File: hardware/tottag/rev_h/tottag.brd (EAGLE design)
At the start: 68.1 x 39.6 mm, 203 parts, among them J1 USB4110-GF-A, J2 DM3AT-SF-PEJM5, J3 TC2030-JLINK-NL-2SIDE, J4 TC2030-JLINK-NL-2SIDE, J5 MOLEX-PICO-SPOX-3SIDE, Q1 CSD75207W15, Q2 CSD75207W15, T1 HHM1595A1, U1 DW1000, U10 STM32F091CC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

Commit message: rev_h: split SPI buses; replace coil
Pin updates from SPI reconfiguration:

    SPI0 (Accelerometer)
        SCLK: P0.17
        MISO: P0.15
        MOSI: P0.13
        (INT, CS pins unchanged)
    SPI2 (RTC, SD Card)
        SCLK: P0.06
        MOSI: P0.07
        MISO: P0.05
        (CS, detect, etc pins unchanged)
    BATIN moved to P0.04 (to simplify routing)

---

Coil replaced with new part; slightly wider holes, adjusted fill to fit

(was meant to be its own commit; oh well)
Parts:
- L4: value WR222230-26M8-G -> WURTH_COIL_760308103204; device ac:WR222230-26M8-G -> ac:WURTH_COIL_760308103204
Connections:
- removed net NRF_MISO: J2.7, R32.1, U11.6, U3.3, U7.AD10
- removed net NRF_MOSI: J2.3, R30.1, U11.9, U3.4, U7.AD8
- removed net NRF_SCK: J2.5, U11.7, U3.1, U7.AD12
- new net NRF_SPI0_MISO: U3.3, U7.AD10
- new net NRF_SPI0_MOSI: U3.4, U7.AD8
- new net NRF_SPI0_SCLK: U3.1, U7.AD12
- new net NRF_SPI2_MISO: J2.7, R32.1, U11.6, U7.K2
- new net NRF_SPI2_MOSI: J2.3, R30.1, U11.9, U7.M2
- new net NRF_SPI2_SCLK: J2.5, U11.7, U7.L1
- net BATIN: now also U7.J1; no longer U7.B9
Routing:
- net NRF_MOSI: track 67.9 -> 0.00 mm, vias 11 -> 0
- net NRF_MISO: track 67.8 -> 0.00 mm, vias 5 -> 0
- net NRF_SCK: track 62.0 -> 0.00 mm, vias 8 -> 0
- net NRF_SPI2_MOSI: track 0.00 -> 56.0 mm, vias 0 -> 9
- net NRF_SPI2_MISO: track 0.00 -> 49.1 mm, vias 0 -> 4
- net NRF_SPI2_SCLK: track 0.00 -> 46.4 mm, vias 0 -> 6
- net NRF_SPI0_MOSI: track 0.00 -> 10.7 mm, vias 0 -> 2
- net NRF_SPI0_SCLK: track 0.00 -> 10.3 mm, vias 0 -> 2
- net NRF_SPI0_MISO: track 0.00 -> 10.2 mm, vias 0 -> 2
- net !NRF_CS_IMU: track 11.7 -> 7.53 mm, vias 4 -> 2
- net BATIN: track 30.3 -> 26.9 mm
- net !NRF_RST: track 30.4 -> 28.9 mm
- net STM_INTERRUPT: track 11.5 -> 12.1 mm

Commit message: rev_h: separate debugging headers; also LEDs
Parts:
- moved J4 8.67 mm to (29.1, -2.69), turned to 0 degrees
- moved D2 8.41 mm to (28.4, 7.21), turned to 270 degrees
- moved D3 1.63 mm to (28.4, 0.25)
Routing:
- net N$60: track 35.6 -> 23.2 mm, vias 3 -> 2
- net N$61: track 34.2 -> 22.4 mm
- net N$59: track 35.5 -> 25.3 mm, vias 4 -> 3
- net !STM_RST: track 33.4 -> 42.8 mm, vias 2 -> 3
- net STM_SWDCLK: track 23.3 -> 30.0 mm
- net N$24: track 32.1 -> 25.4 mm
- net STM_SWDIO: track 29.3 -> 35.5 mm
- net N$23: track 29.0 -> 22.9 mm
- net GND: track 185.9 -> 191.3 mm, vias 553 -> 551
- net N$25: track 29.2 -> 24.7 mm
- net !NRF_RST: track 28.9 -> 31.7 mm, vias 4 -> 3
- net NRF_SWDIO: track 32.5 -> 29.7 mm, vias 2 -> 1
- net +3V3: track 145.3 -> 147.9 mm, vias 42 -> 46
- net NRF_SWDCLK: track 26.4 -> 28.7 mm, vias 2 -> 1
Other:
- outline, holes or cut-outs redrawn

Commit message: rev_h: add board ID pins
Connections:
- net +3V3: now also U7.AC15
- net GND: now also U7.AC17, U7.AC19
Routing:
- net GND: track 191.3 -> 192.8 mm
- net +3V3: track 147.9 -> 148.4 mm
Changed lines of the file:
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@@
 <wire x1="32.1056" y1="0.6096" x2="30.3276" y2="-1.1684" width="0.6096" layer="16"/>
 <wire x1="30.3276" y1="-1.1684" x2="30.3276" y2="-2.0574" width="0.6096" layer="16"/>
+<contactref element="U7" pad="AC19"/>
+<contactref element="U7" pad="AC17"/>
+<wire x1="15.089" y1="17.5954" x2="15.089" y2="18.137" width="0.1524" layer="1"/>
+<wire x1="15.089" y1="18.137" x2="15.4178" y2="18.4658" width="0.1524" layer="1"/>
+<wire x1="15.089" y1="17.5954" x2="14.589" y2="17.5954" width="0.1524" layer="1"/>
 </signal>
 <signal name="VUSB">
@@
 <wire x1="28.9052" y1="1.8288" x2="28.9052" y2="1.8796" width="0.3048" layer="15"/>
 <wire x1="28.9052" y1="1.8796" x2="29.6672" y2="2.6416" width="0.3048" layer="15"/>
+<contactref element="U7" pad="AC15"/>
+<wire x1="13.839" y1="17.0954" x2="14.089" y2="17.5954" width="0.1524" layer="1"/>
 </signal>
 <signal name="N$22">

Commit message: rev_h: RTC CS pull-up to +3v3
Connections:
- net +3V3: now also R34.1
- net VBAT_RTC: no longer R34.1
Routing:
- net VBAT_RTC: track 7.64 -> 6.12 mm
- net +3V3: track 148.4 -> 149.1 mm, vias 46 -> 47
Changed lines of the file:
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@@
 <via x="9.906" y="29.972" extent="1-16" drill="0.2032"/>
 <via x="19.6596" y="27.8892" extent="1-16" drill="0.2032"/>
-<via x="18.4658" y="29.9212" extent="1-16" drill="0.2032"/>
+<via x="18.415" y="29.972" extent="1-16" drill="0.2032"/>
 <via x="13.97" y="29.972" extent="1-16" drill="0.2032"/>
 <via x="11.43" y="29.972" extent="1-16" drill="0.2032"/>
@@
 <contactref element="U7" pad="AC15"/>
 <wire x1="13.839" y1="17.0954" x2="14.089" y2="17.5954" width="0.1524" layer="1"/>
+<contactref element="R34" pad="1"/>
+<wire x1="18.82266875" y1="29.0576" x2="18.82266875" y2="29.59226875" width="0.2032" layer="1"/>
+<wire x1="18.82266875" y1="29.59226875" x2="18.8976" y2="29.6672" width="0.2032" layer="1"/>
+<via x="18.8976" y="29.6672" extent="1-16" drill="0.2032"/>
 </signal>
 <signal name="N$22">
@@
 <contactref element="U11" pad="5"/>
 <contactref element="R16" pad="1"/>
-<wire x1="21.94433125" y1="29.1592" x2="21.2344" y2="29.1592" width="0.4064" layer="1"/>
-<wire x1="21.2344" y1="29.1592" x2="20.6248" y2="29.7688" width="0.4064" layer="1"/>
-<wire x1="19.812" y1="29.7688" x2="20.6248" y2="29.7688" width="0.4064" layer="1"/>
-<wire x1="18.5928" y1="27.6352" x2="18.5928" y2="27.2288" width="0.3302" layer="1"/>
-<wire x1="18.5928" y1="27.2288" x2="18.5928" y2="26.6042" width="0.254" layer="1"/>
+<wire x1="21.94433125" y1="29.1592" x2="21.2344" y2="29.1592" width="0.2032" layer="1"/>
+<wire x1="21.2344" y1="29.1592" x2="20.6248" y2="29.7688" width="0.2032" layer="1"/>
+<wire x1="19.812" y1="29.7688" x2="20.6248" y2="29.7688" width="0.2032" layer="1"/>
+<wire x1="18.5928" y1="27.6352" x2="18.5928" y2="27.2288" width="0.2032" layer="1"/>
+<wire x1="18.5928" y1="27.2288" x2="18.5928" y2="26.6042" width="0.2032" layer="1"/>
 <wire x1="18.5928" y1="26.6042" x2="18.6406" y2="26.5564" width="0.254" layer="1"/>
-<wire x1="18.5928" y1="27.6352" x2="19.5072" y2="28.5496" width="0.4064" layer="1"/>
-<wire x1="19.5072" y1="28.5496" x2="19.5072" y2="29.464" width="0.4064" layer="1"/>
-<wire x1="19.5072" y1="29.464" x2="19.812" y2="29.7688" width="0.4064" layer="1"/>
-<contactref element="R34" pad="1"/>
-<wire x1="18.82266875" y1="29.0576" x2="18.5928" y2="28.82773125" width="0.2032" layer="1"/>
-<wire x1="18.5928" y1="28.82773125" x2="18.5928" y2="27.6352" width="0.2032" layer="1"/>
+<wire x1="18.5928" y1="27.6352" x2="19.5072" y2="28.5496" width="0.2032" layer="1"/>
+<wire x1="19.5072" y1="28.5496" x2="19.5072" y2="29.464" width="0.2032" layer="1"/>
+<wire x1="19.5072" y1="29.464" x2="19.812" y2="29.7688" width="0.2032" layer="1"/>
 </signal>
 <signal name="N$45">

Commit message: rev_h: move ID pins to low-freq GPIO pins
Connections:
- net +3V3: now also U7.A20; no longer U7.AC15
- net GND: now also U7.B17, U7.B19; no longer U7.AC17, U7.AC19
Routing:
- net GND: track 192.8 -> 195.2 mm, vias 551 -> 550
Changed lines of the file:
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@@
 <via x="12.8778" y="18.4658" extent="1-16" drill="0.2032"/>
 <via x="14.1478" y="18.4658" extent="1-16" drill="0.2032"/>
-<via x="15.4178" y="18.4658" extent="1-16" drill="0.2032"/>
 <via x="24.6888" y="27.051" extent="1-16" drill="0.2032"/>
 <via x="25.3492" y="25.654" extent="1-16" drill="0.2032"/>
@@
 <wire x1="32.1056" y1="0.6096" x2="30.3276" y2="-1.1684" width="0.6096" layer="16"/>
 <wire x1="30.3276" y1="-1.1684" x2="30.3276" y2="-2.0574" width="0.6096" layer="16"/>
-<contactref element="U7" pad="AC19"/>
-<contactref element="U7" pad="AC17"/>
-<wire x1="15.089" y1="17.5954" x2="15.089" y2="18.137" width="0.1524" layer="1"/>
-<wire x1="15.089" y1="18.137" x2="15.4178" y2="18.4658" width="0.1524" layer="1"/>
-<wire x1="15.089" y1="17.5954" x2="14.589" y2="17.5954" width="0.1524" layer="1"/>
+<contactref element="U7" pad="B19" route="any" routetag="G$1.P1.11*"/>
+<contactref element="U7" pad="B17"/>
+<wire x1="14.589" y1="23.0954" x2="15.089" y2="23.0954" width="0.1524" layer="1"/>
+<wire x1="13.589" y1="20.3454" x2="15.089" y2="21.8454" width="0.1524" layer="1"/>
+<wire x1="15.089" y1="21.8454" x2="15.089" y2="23.0954" width="0.1524" layer="1"/>
 </signal>
 <signal name="VUSB">
@@
 <wire x1="28.9052" y1="1.8288" x2="28.9052" y2="1.8796" width="0.3048" layer="15"/>
 <wire x1="28.9052" y1="1.8796" x2="29.6672" y2="2.6416" width="0.3048" layer="15"/>
-<contactref element="U7" pad="AC15"/>
-<wire x1="13.839" y1="17.0954" x2="14.089" y2="17.5954" width="0.1524" layer="1"/>
 <contactref element="R34" pad="1"/>
 <wire x1="18.82266875" y1="29.0576" x2="18.82266875" y2="29.59226875" width="0.2032" layer="1"/>
 <wire x1="18.82266875" y1="29.59226875" x2="18.8976" y2="29.6672" width="0.2032" layer="1"/>
 <via x="18.8976" y="29.6672" extent="1-16" drill="0.2032"/>
+<contactref element="U7" pad="A20"/>
+<wire x1="15.339" y1="23.5954" x2="15.839" y2="23.5954" width="0.1524" layer="1"/>
 </signal>
 <signal name="N$22">

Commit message: rev_h: add test points for all buses
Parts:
- added TP19, TP20, TP21, TP22, TP23, TP24, TP25, TP26, TP27: TEST-POINT, headers:PAD.03X.03
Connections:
- net !NRF_CS_IMU: now also TP22.P$1
- net !NRF_CS_RTC: now also TP27.P$1
- net !NRF_CS_SD: now also TP26.P$1
- net NRF_SPI0_MISO: now also TP21.P$1
- net NRF_SPI0_MOSI: now also TP20.P$1
- net NRF_SPI0_SCLK: now also TP19.P$1
- net NRF_SPI2_MISO: now also TP25.P$1
- net NRF_SPI2_MOSI: now also TP24.P$1
- net NRF_SPI2_SCLK: now also TP23.P$1
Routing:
- net !NRF_CS_SD: track 44.2 -> 59.7 mm
- net NRF_SPI2_MISO: track 49.1 -> 62.8 mm, vias 4 -> 5
- net NRF_SPI2_MOSI: track 56.0 -> 67.1 mm
- net NRF_SPI2_SCLK: track 46.4 -> 55.5 mm, vias 6 -> 7
- net !NRF_CS_IMU: track 7.53 -> 12.0 mm
- net NRF_SPI0_SCLK: track 10.3 -> 12.5 mm
- net NRF_SPI0_MOSI: track 10.7 -> 12.4 mm
- net NRF_SPI0_MISO: track 10.2 -> 11.5 mm
- net !NRF_CS_RTC: track 15.3 -> 16.1 mm
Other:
- board text added: "MISO"
- board text added: "MOSI"
- board text added: "SCLK"
- board text added: "nCS"

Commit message: rev_h: Connect STM PA0 to allow STANDBY wake
Slightly unclear whether STM should allow for STANDBY wake from any
of the WKUP pins, but some forum posts indicate that it can actually
only be done from WKUP1 for STANDBY mode. In either case, another
GPIO link between the two micro's isn't a huge deal.

This does sacrifice the GPIO1 test point from the nRF, because getting
at any other pin would've been insane.
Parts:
- removed TP14: TEST-POINT, headers:PAD.03X.03
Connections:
- removed net NRF_GPIO_1: TP14.P$1, U7.G1
- new net STM_WKUP1: U10.10, U7.G1
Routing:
- net STM_WKUP1: track 0.00 -> 11.1 mm, vias 0 -> 2
- net NRF_GPIO_1: track 6.81 -> 0.00 mm, vias 2 -> 0
- net GND: track 195.2 -> 196.0 mm
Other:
- board text removed: "GPIO1"

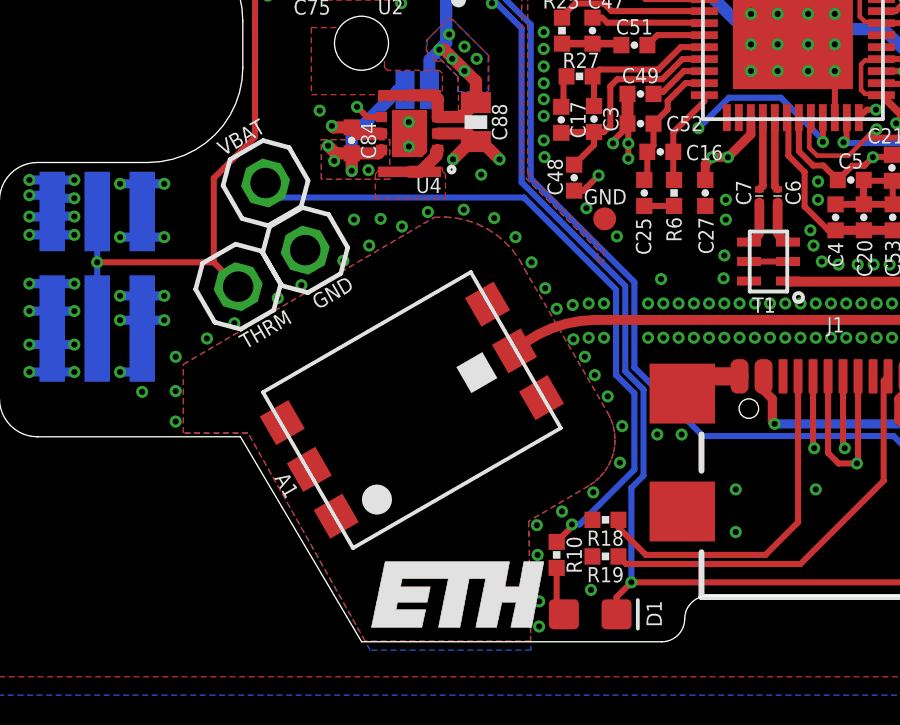
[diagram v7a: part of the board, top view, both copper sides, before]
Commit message: rev_h: tie !CHG LED to +3v3
This means the LED won't power on to indicate charging if the device
is switched off, but that's an uncommon case anyway. We may even end
up just DNP'ing the CHG LED; it's of middling use; in which case an
internal nRF pull-up can be used in place of this for the !CHG net.
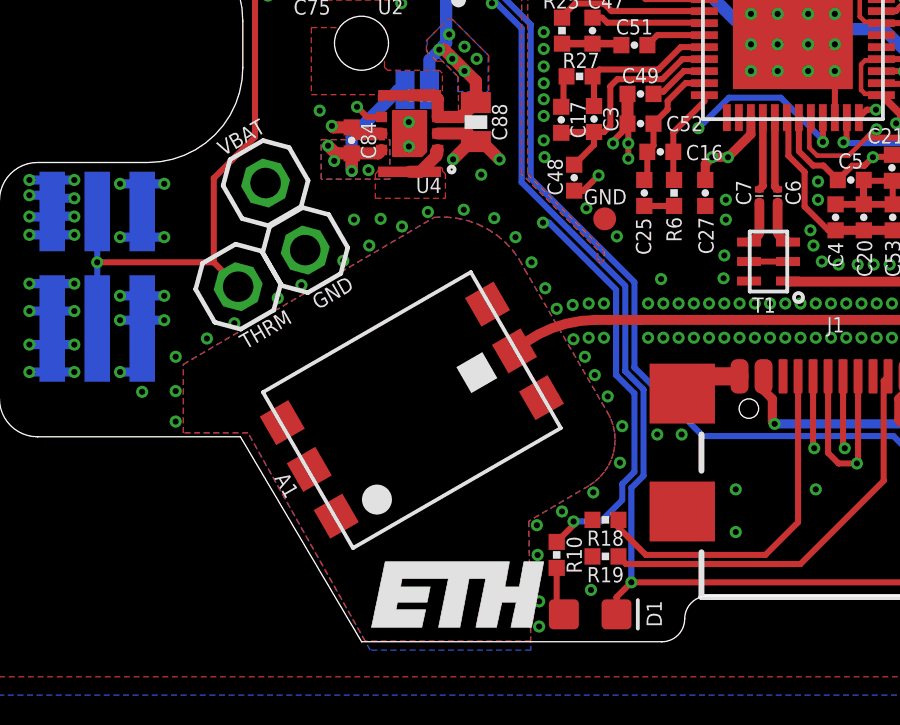
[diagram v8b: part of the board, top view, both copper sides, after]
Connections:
- net +3V3: now also R10.1
- net VBAT: no longer R10.1
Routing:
- net VBAT: track 83.4 -> 60.3 mm, vias 30 -> 29
- net +3V3: track 149.1 -> 162.7 mm, vias 47 -> 49
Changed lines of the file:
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@@
 <layer number="10" name="Route10" color="1" fill="7" visible="no" active="no"/>
 <layer number="11" name="Route11" color="4" fill="7" visible="no" active="no"/>
-<layer number="12" name="Route12" color="1" fill="5" visible="no" active="yes"/>
+<layer number="12" name="Route12" color="1" fill="5" visible="yes" active="yes"/>
 <layer number="13" name="Route13" color="4" fill="5" visible="no" active="no"/>
 <layer number="14" name="Route14" color="1" fill="6" visible="no" active="no"/>
@@
 <contactref element="S1" pad="2"/>
 <contactref element="U2" pad="10"/>
-<contactref element="R10" pad="1"/>
 <wire x1="-21.1328" y1="20.7832" x2="-21.1328" y2="15.7988" width="0.8128" layer="15"/>
 <wire x1="-25.0444" y1="13.1318" x2="-22.86" y2="15.3162" width="0.8128" layer="15" curve="-90"/>
-<wire x1="-15.494" y1="-3.12293125" x2="-14.986" y2="-2.61493125" width="0.2032" layer="1"/>
-<wire x1="-14.986" y1="-2.54" x2="-14.986" y2="-2.61493125" width="0.2032" layer="1"/>
-<via x="-14.986" y="-2.54" extent="1-16" drill="0.2032"/>
-<wire x1="-14.986" y1="-2.54" x2="-14.732" y2="-2.54" width="0.2032" layer="16"/>
-<wire x1="-12.9032" y1="-0.7112" x2="-12.9032" y2="1.8288" width="0.2032" layer="16"/>
-<wire x1="-12.9032" y1="1.8288" x2="-13.5128" y2="2.4384" width="0.2032" layer="16"/>
-<wire x1="-13.5128" y1="2.4384" x2="-13.5128" y2="5.2832" width="0.2032" layer="16"/>
-<wire x1="-13.5128" y1="5.2832" x2="-16.5862" y2="8.3566" width="0.2032" layer="16"/>
-<wire x1="-14.732" y1="-2.54" x2="-12.9032" y2="-0.7112" width="0.2032" layer="16"/>
 <contactref element="C75" pad="1"/>
 <contactref element="J6" pad="1"/>
 <wire x1="-25.0444" y1="8.9916" x2="-25.1968" y2="8.8392" width="0.8128" layer="15"/>
 <wire x1="-25.0444" y1="13.1318" x2="-25.0444" y2="8.9916" width="0.8128" layer="15"/>
-<wire x1="-24.7142" y1="8.3566" x2="-25.1968" y2="8.8392" width="0.2032" layer="16"/>
-<wire x1="-16.5862" y1="8.3566" x2="-24.7142" y2="8.3566" width="0.2032" layer="16"/>
 <contactref element="R35" pad="2"/>
 <polygon width="0.0508" layer="1" thermals="no">
@@
 <contactref element="U7" pad="A20"/>
 <wire x1="15.339" y1="23.5954" x2="15.839" y2="23.5954" width="0.1524" layer="1"/>
+<contactref element="R10" pad="1"/>
+<wire x1="-15.494" y1="-3.12293125" x2="-14.9315875" y2="-2.56051875" width="0.2032" layer="1"/>
+<wire x1="-14.9315875" y1="-2.56051875" x2="-14.9315875" y2="-2.4420125" width="0.2032" layer="1"/>
+<via x="-14.9315875" y="-2.4420125" extent="1-16" drill="0.2032"/>
+<wire x1="-14.9315875" y1="-2.4420125" x2="-14.927975" y2="-2.4384" width="0.2032" layer="16"/>
+<wire x1="-14.927975" y1="-2.4384" x2="-14.0208" y2="-2.4384" width="0.2032" layer="16"/>
+<wire x1="-14.0208" y1="-2.4384" x2="-13.3096" y2="-1.7272" width="0.2032" layer="16"/>
+<wire x1="-13.3096" y1="-1.7272" x2="-13.3096" y2="-1.19454375" width="0.2032" layer="16"/>
+<wire x1="-12.9032" y1="-0.78814375" x2="-12.9032" y2="1.8288" width="0.2032" layer="16"/>
+<wire x1="-13.3096" y1="-1.19454375" x2="-12.9032" y2="-0.78814375" width="0.2032" layer="16"/>
+<wire x1="-12.9032" y1="1.8288" x2="-13.5128" y2="2.4384" width="0.2032" layer="16"/>
+<wire x1="-13.5128" y1="2.4384" x2="-13.5128" y2="5.2832" width="0.2032" layer="16"/>
+<wire x1="-15.748" y1="7.5184" x2="-15.9512" y2="7.5184" width="0.2032" layer="16"/>
+<via x="-15.9512" y="7.5184" extent="1-16" drill="0.2032"/>
+<wire x1="-13.5128" y1="5.2832" x2="-15.748" y2="7.5184" width="0.2032" layer="16"/>
 </signal>
 <signal name="N$22">
